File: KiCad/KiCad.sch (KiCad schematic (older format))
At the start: 18 parts, among them J1 HV input, U1 PQMC3-D12-S12-S, U2 LM311N_NOPB

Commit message: Schematic Complete
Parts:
- added C2, C5: 1u, symbol Device:C
- added C3, C4: 100n, symbol Device:C
- added D2: D, symbol Device:D
- added D3: LEDR, symbol Device:LED
- added J2: Conn_01x05_Female, symbol Connector:Conn_01x05_Female
- added Q1, Q3: 2N7002, digikey-footprints:SOT-23-3, symbol dk_Transistors-FETs-MOSFETs-Single:2N7002
- added Q2, Q4: MCT06P10-TP, symbol Lukas_Library:MCT06P10-TP
- added R13: 1k, symbol Device:R
- added R14, R15: 22k, symbol Device:R
- added R16: 220k, symbol Device:R
- added R17: 10k, symbol Device:R
- added R18: 2k, symbol Device:R
- added U4: NE555, symbol Timer:NE555
- C1: value C -> 10n
- gave numbers to parts that had none: 2
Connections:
- net GLV-: now reaches U1.1 (-Vin)
- net GLV-: now also C2.1, C3.2, C4.2, C5.2, J2.4 (Pin_4), J2.5 (Pin_5), Q1.2 (S), Q3.2 (S), R13.2, R18.1, U4.1 (GND)
- net VCC: now reaches U1.2 (+Vin)
- net VCC: now also U3.5, C2.2, C3.1, D2.1 (K), R14.1, R15.1, U4.8 (VCC)
- net at U3.4: now also Q1.1 (G), R13.1
- new net: C5.1, R16.1, U4.2 (TR), U4.6 (THR)
- new net: Q3.1 (G), U4.3 (Q)
- new net: Q1.3 (D), Q2.1 (G), R14.2, U4.4 (R)
- new net: C4.1, U4.5 (CV)
- new net: R15.2, R16.2, U4.7 (DIS)
- new net: Q3.3 (D), R17.2
- new net: Q4.1 (G), R17.1
- new net: D3.1 (K), R18.2
- new net GLV+: D2.2 (A), J2.1 (Pin_1), Q2.3 (D), Q4.3 (D)
- new net GRN+: J2.2 (Pin_2), Q2.2 (S)
- new net RED+: D3.2 (A), J2.3 (Pin_3), Q4.2 (S)
- no-connect marks 1 -> 2

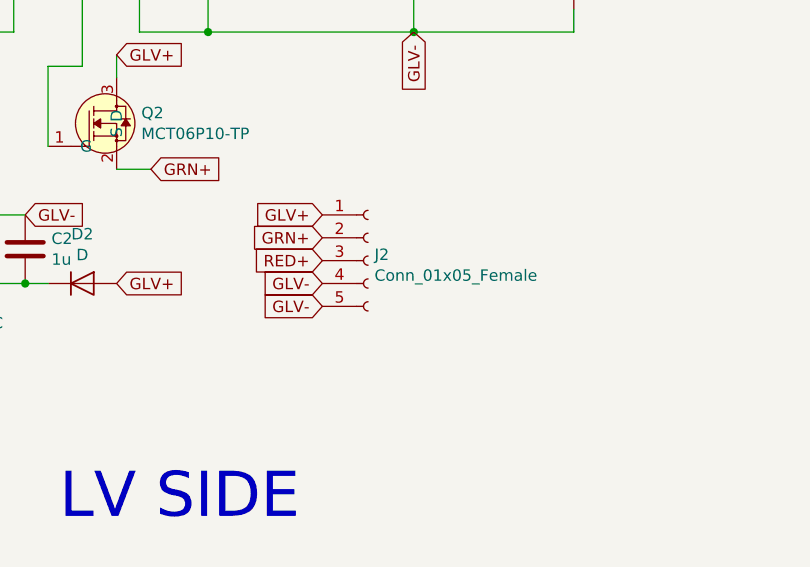
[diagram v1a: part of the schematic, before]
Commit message: changed pins
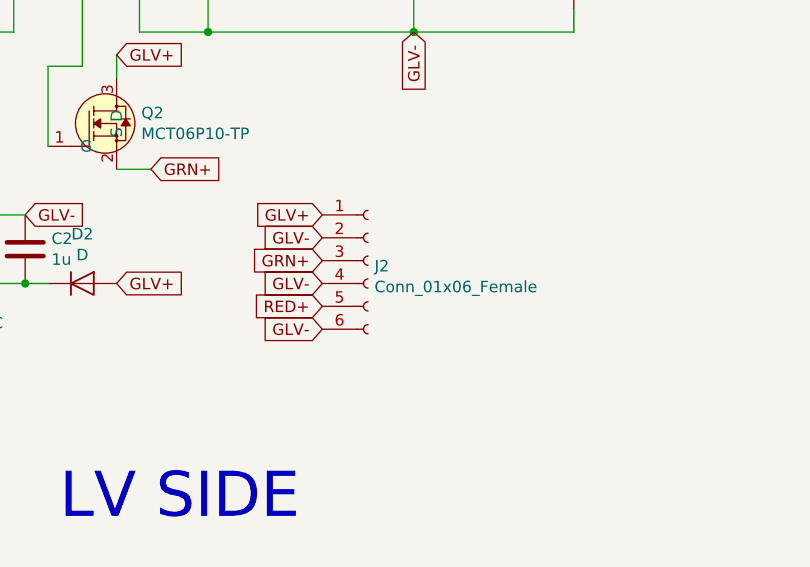
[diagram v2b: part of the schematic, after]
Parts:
- removed J2: Conn_01x05_Female, symbol Connector:Conn_01x05_Female
- added J2: Conn_01x06_Female, symbol Connector:Conn_01x06_Female
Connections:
- net GLV+: now also J2.1 (Pin_1)
- net GLV-: now also J2.2 (Pin_2), J2.4 (Pin_4), J2.6 (Pin_6)
- net GRN+: now also J2.3 (Pin_3)
- net RED+: now also J2.5 (Pin_5)
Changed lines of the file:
@@
 	1    0    0    -1
 $EndComp
-$Comp
-L Connector:Conn_01x05_Female J2
-U 1 1 60B41F0A
-P 8350 5200
-F 0 "J2" H 8378 5226 50  0000 L CNN
-F 1 "Conn_01x05_Female" H 8378 5135 50  0000 L CNN
-F 2 "" H 8350 5200 50  0001 C CNN
-F 3 "~" H 8350 5200 50  0001 C CNN
-	1    8350 5200
-	1    0    0    -1
-$EndComp
-Text GLabel 8150 5400 0    50   Input ~ 0
+Text GLabel 8150 5100 0    50   Input ~ 0
 GLV-
 Text GLabel 8150 5000 0    50   Input ~ 0
 GLV+
-Text GLabel 8150 5100 0    50   Input ~ 0
+Text GLabel 8150 5200 0    50   Input ~ 0
 GRN+
-Text GLabel 8150 5200 0    50   Input ~ 0
+Text GLabel 8150 5400 0    50   Input ~ 0
 RED+
 $Comp
@@
 Text GLabel 7250 5300 2    50   Input ~ 0
 GLV+
-Text GLabel 8150 5300 0    50   Input ~ 0
+Text GLabel 8150 5500 0    50   Input ~ 0
 GLV-
 Text GLabel 6850 5000 2    50   Input ~ 0
@@
 Wire Wire Line
 	10450 2950 10500 2950
+$Comp
+L Connector:Conn_01x06_Female J2
+U 1 1 60B46070
+P 8350 5200
+F 0 "J2" H 8378 5176 50  0000 L CNN
+F 1 "Conn_01x06_Female" H 8378 5085 50  0000 L CNN
+F 2 "" H 8350 5200 50  0001 C CNN
+F 3 "~" H 8350 5200 50  0001 C CNN
+	1    8350 5200
+	1    0    0    -1
+$EndComp
+Text GLabel 8150 5300 0    50   Input ~ 0
+GLV-
 $EndSCHEMATC

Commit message: Footprints
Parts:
- C1, C2, C3, C4, C5: footprint (none) -> Capacitor_SMD:C_0603_1608Metric_Pad1.05x0.95mm_HandSolder
- D1, D2: footprint (none) -> Diode_SMD:D_0603_1608Metric_Pad1.05x0.95mm_HandSolder
- D3: footprint (none) -> LED_SMD:LED_0603_1608Metric_Pad1.05x0.95mm_HandSolder
- Q2, Q4: footprint (none) -> Package_TO_SOT_SMD:SOT-223
- R1, R2, R3, R4: footprint (none) -> Resistor_SMD:R_2512_6332Metric_Pad1.52x3.35mm_HandSolder
- R10, R12, R13, R14, R15, R16, R17, R18, R5, R6, R7, R8, R9: footprint (none) -> Resistor_SMD:R_0603_1608Metric_Pad1.05x0.95mm_HandSolder
- R11: footprint (none) -> Resistor_SMD:R_0805_2012Metric_Pad1.15x1.40mm_HandSolder
- U4: footprint (none) -> Package_DIP:DIP-8_W7.62mm
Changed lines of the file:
@@
 F 0 "R1" V 1293 950 50  0000 C CNN
 F 1 "250k" V 1384 950 50  0000 C CNN
-F 2 "" V 1430 950 50  0001 C CNN
+F 2 "Resistor_SMD:R_2512_6332Metric_Pad1.52x3.35mm_HandSolder" V 1430 950 50  0001 C CNN
 F 3 "~" H 1500 950 50  0001 C CNN
 	1    1500 950
@@
 F 0 "R2" V 1693 950 50  0000 C CNN
 F 1 "250k" V 1784 950 50  0000 C CNN
-F 2 "" V 1830 950 50  0001 C CNN
+F 2 "Resistor_SMD:R_2512_6332Metric_Pad1.52x3.35mm_HandSolder" V 1830 950 50  0001 C CNN
 F 3 "~" H 1900 950 50  0001 C CNN
 	1    1900 950
@@
 F 0 "R3" V 2093 950 50  0000 C CNN
 F 1 "250k" V 2184 950 50  0000 C CNN
-F 2 "" V 2230 950 50  0001 C CNN
+F 2 "Resistor_SMD:R_2512_6332Metric_Pad1.52x3.35mm_HandSolder" V 2230 950 50  0001 C CNN
 F 3 "~" H 2300 950 50  0001 C CNN
 	1    2300 950
@@
 F 0 "R4" V 2493 950 50  0000 C CNN
 F 1 "200k" V 2584 950 50  0000 C CNN
-F 2 "" V 2630 950 50  0001 C CNN
+F 2 "Resistor_SMD:R_2512_6332Metric_Pad1.52x3.35mm_HandSolder" V 2630 950 50  0001 C CNN
 F 3 "~" H 2700 950 50  0001 C CNN
 	1    2700 950
@@
 F 0 "R6" H 3180 1354 50  0000 R CNN
 F 1 "50k" H 3180 1445 50  0000 R CNN
-F 2 "" V 3180 1400 50  0001 C CNN
+F 2 "Resistor_SMD:R_0603_1608Metric_Pad1.05x0.95mm_HandSolder" V 3180 1400 50  0001 C CNN
 F 3 "~" H 3250 1400 50  0001 C CNN
 	1    3250 1400
@@
 F 0 "D1" V 3804 1329 50  0000 L CNN
 F 1 "12V" V 3895 1329 50  0000 L CNN
-F 2 "" H 3850 1250 50  0001 C CNN
+F 2 "Diode_SMD:D_0603_1608Metric_Pad1.05x0.95mm_HandSolder" H 3850 1250 50  0001 C CNN
 F 3 "~" H 3850 1250 50  0001 C CNN
 	1    3850 1250
@@
 F 0 "R5" V 1643 2100 50  0000 C CNN
 F 1 "75k" V 1734 2100 50  0000 C CNN
-F 2 "" V 1780 2100 50  0001 C CNN
+F 2 "Resistor_SMD:R_0603_1608Metric_Pad1.05x0.95mm_HandSolder" V 1780 2100 50  0001 C CNN
 F 3 "~" H 1850 2100 50  0001 C CNN
 	1    1850 2100
@@
 F 0 "R8" V 2093 2100 50  0000 C CNN
 F 1 "24k" V 2184 2100 50  0000 C CNN
-F 2 "" V 2230 2100 50  0001 C CNN
+F 2 "Resistor_SMD:R_0603_1608Metric_Pad1.05x0.95mm_HandSolder" V 2230 2100 50  0001 C CNN
 F 3 "~" H 2300 2100 50  0001 C CNN
 	1    2300 2100
@@
 F 0 "R9" V 2793 2100 50  0000 C CNN
 F 1 "900" V 2884 2100 50  0000 C CNN
-F 2 "" V 2930 2100 50  0001 C CNN
+F 2 "Resistor_SMD:R_0603_1608Metric_Pad1.05x0.95mm_HandSolder" V 2930 2100 50  0001 C CNN
 F 3 "~" H 3000 2100 50  0001 C CNN
 	1    3000 2100
@@
 F 0 "R7" H 1980 2604 50  0000 R CNN
 F 1 "100" H 1980 2695 50  0000 R CNN
-F 2 "" V 1980 2650 50  0001 C CNN
+F 2 "Resistor_SMD:R_0603_1608Metric_Pad1.05x0.95mm_HandSolder" V 1980 2650 50  0001 C CNN
 F 3 "~" H 2050 2650 50  0001 C CNN
 	1    2050 2650
@@
 F 0 "R10" V 4457 1100 50  0000 C CNN
 F 1 "100" V 4366 1100 50  0000 C CNN
-F 2 "" V 4180 1100 50  0001 C CNN
+F 2 "Resistor_SMD:R_0603_1608Metric_Pad1.05x0.95mm_HandSolder" V 4180 1100 50  0001 C CNN
 F 3 "~" H 4250 1100 50  0001 C CNN
 	1    4250 1100
@@
 F 0 "C1" H 3765 4446 50  0000 L CNN
 F 1 "10n" H 3765 4355 50  0000 L CNN
-F 2 "" H 3688 4250 50  0001 C CNN
+F 2 "Capacitor_SMD:C_0603_1608Metric_Pad1.05x0.95mm_HandSolder" H 3688 4250 50  0001 C CNN
 F 3 "~" H 3650 4400 50  0001 C CNN
 	1    3650 4400
@@
 F 0 "R11" V 4507 3550 50  0000 C CNN
 F 1 "1M" V 4416 3550 50  0000 C CNN
-F 2 "" V 4230 3550 50  0001 C CNN
+F 2 "Resistor_SMD:R_0805_2012Metric_Pad1.15x1.40mm_HandSolder" V 4230 3550 50  0001 C CNN
 F 3 "~" H 4300 3550 50  0001 C CNN
 	1    4300 3550
@@
 F 0 "R12" H 5670 3296 50  0000 L CNN
 F 1 "2k" H 5670 3205 50  0000 L CNN
-F 2 "" V 5530 3250 50  0001 C CNN
+F 2 "Resistor_SMD:R_0603_1608Metric_Pad1.05x0.95mm_HandSolder" V 5530 3250 50  0001 C CNN
 F 3 "~" H 5600 3250 50  0001 C CNN
 	1    5600 3250
@@
 F 0 "U4" H 8550 3781 50  0000 C CNN
 F 1 "NE555" H 8550 3690 50  0000 C CNN
-F 2 "" H 8550 3200 50  0001 C CNN
+F 2 "Package_DIP:DIP-8_W7.62mm" H 8550 3200 50  0001 C CNN
 F 3 "http://www.ti.com/lit/ds/symlink/ne555.pdf" H 8550 3200 50  0001 C CNN
 	1    8550 3200
@@
 F 0 "C2" H 6965 5196 50  0000 L CNN
 F 1 "1u" H 6965 5105 50  0000 L CNN
-F 2 "" H 6888 5000 50  0001 C CNN
+F 2 "Capacitor_SMD:C_0603_1608Metric_Pad1.05x0.95mm_HandSolder" H 6888 5000 50  0001 C CNN
 F 3 "~" H 6850 5150 50  0001 C CNN
 	1    6850 5150
@@
 F 0 "D2" H 7100 5516 50  0000 C CNN
 F 1 "D" H 7100 5425 50  0000 C CNN
-F 2 "" H 7100 5300 50  0001 C CNN
+F 2 "Diode_SMD:D_0603_1608Metric_Pad1.05x0.95mm_HandSolder" H 7100 5300 50  0001 C CNN
 F 3 "~" H 7100 5300 50  0001 C CNN
 	1    7100 5300
@@
 F 0 "R13" H 6370 4096 50  0000 L CNN
 F 1 "1k" H 6370 4005 50  0000 L CNN
-F 2 "" V 6230 4050 50  0001 C CNN
+F 2 "Resistor_SMD:R_0603_1608Metric_Pad1.05x0.95mm_HandSolder" V 6230 4050 50  0001 C CNN
 F 3 "~" H 6300 4050 50  0001 C CNN
 	1    6300 4050
@@
 F 0 "R14" H 6870 2946 50  0000 L CNN
 F 1 "22k" H 6870 2855 50  0000 L CNN
-F 2 "" V 6730 2900 50  0001 C CNN
+F 2 "Resistor_SMD:R_0603_1608Metric_Pad1.05x0.95mm_HandSolder" V 6730 2900 50  0001 C CNN
 F 3 "~" H 6800 2900 50  0001 C CNN
 	1    6800 2900
@@
 F 0 "C3" H 7465 3896 50  0000 L CNN
 F 1 "100n" H 7465 3805 50  0000 L CNN
-F 2 "" H 7388 3700 50  0001 C CNN
+F 2 "Capacitor_SMD:C_0603_1608Metric_Pad1.05x0.95mm_HandSolder" H 7388 3700 50  0001 C CNN
 F 3 "~" H 7350 3850 50  0001 C CNN
 	1    7350 3850
@@
 F 0 "C4" H 7765 3896 50  0000 L CNN
 F 1 "100n" H 7765 3805 50  0000 L CNN
-F 2 "" H 7688 3700 50  0001 C CNN
+F 2 "Capacitor_SMD:C_0603_1608Metric_Pad1.05x0.95mm_HandSolder" H 7688 3700 50  0001 C CNN
 F 3 "~" H 7650 3850 50  0001 C CNN
 	1    7650 3850
@@
 F 0 "R15" H 9370 2746 50  0000 L CNN
 F 1 "22k" H 9370 2655 50  0000 L CNN
-F 2 "" V 9230 2700 50  0001 C CNN
+F 2 "Resistor_SMD:R_0603_1608Metric_Pad1.05x0.95mm_HandSolder" V 9230 2700 50  0001 C CNN
 F 3 "~" H 9300 2700 50  0001 C CNN
 	1    9300 2700
@@
 F 0 "R16" H 9370 3396 50  0000 L CNN
 F 1 "220k" H 9370 3305 50  0000 L CNN
-F 2 "" V 9230 3350 50  0001 C CNN
+F 2 "Resistor_SMD:R_0603_1608Metric_Pad1.05x0.95mm_HandSolder" V 9230 3350 50  0001 C CNN
 F 3 "~" H 9300 3350 50  0001 C CNN
 	1    9300 3350
@@
 F 0 "C5" H 9365 3996 50  0000 L CNN
 F 1 "1u" H 9365 3905 50  0000 L CNN
-F 2 "" H 9288 3800 50  0001 C CNN
+F 2 "Capacitor_SMD:C_0603_1608Metric_Pad1.05x0.95mm_HandSolder" H 9288 3800 50  0001 C CNN
 F 3 "~" H 9250 3950 50  0001 C CNN
 	1    9250 3950
@@
 F 0 "R17" H 9920 2496 50  0000 L CNN
 F 1 "10k" H 9920 2405 50  0000 L CNN
-F 2 "" V 9780 2450 50  0001 C CNN
+F 2 "Resistor_SMD:R_0603_1608Metric_Pad1.05x0.95mm_HandSolder" V 9780 2450 50  0001 C CNN
 F 3 "~" H 9850 2450 50  0001 C CNN
 	1    9850 2450
@@
 F 0 "R18" H 11020 2996 50  0000 L CNN
 F 1 "2k" H 11020 2905 50  0000 L CNN
-F 2 "" V 10880 2950 50  0001 C CNN
+F 2 "Resistor_SMD:R_0603_1608Metric_Pad1.05x0.95mm_HandSolder" V 10880 2950 50  0001 C CNN
 F 3 "~" H 10950 2950 50  0001 C CNN
 	1    10950 2950
@@
 F 0 "D3" H 10643 2695 50  0000 C CNN
 F 1 "LEDR" H 10643 2786 50  0000 C CNN
-F 2 "" H 10650 2950 50  0001 C CNN
+F 2 "LED_SMD:LED_0603_1608Metric_Pad1.05x0.95mm_HandSolder" H 10650 2950 50  0001 C CNN
 F 3 "~" H 10650 2950 50  0001 C CNN
 	1    10650 2950
@@
 F 0 "Q2" H 7358 3846 50  0000 L CNN
 F 1 "MCT06P10-TP" H 7358 3755 50  0000 L CNN
-F 2 "" H 7200 3600 50  0001 C CNN
+F 2 "Package_TO_SOT_SMD:SOT-223" H 7200 3600 50  0001 C CNN
 F 3 "https://www.digikey.ca/en/products/detail/micro-commercial-co/MCT06P10-TP/10054363" H 7200 3600 50  0001 C CNN
 	1    7200 4200
@@
 F 0 "Q4" H 10308 1346 50  0000 L CNN
 F 1 "MCT06P10-TP" H 10308 1255 50  0000 L CNN
-F 2 "" H 10150 1100 50  0001 C CNN
+F 2 "Package_TO_SOT_SMD:SOT-223" H 10150 1100 50  0001 C CNN
 F 3 "https://www.digikey.ca/en/products/detail/micro-commercial-co/MCT06P10-TP/10054363" H 10150 1100 50  0001 C CNN
 	1    10150 1700
